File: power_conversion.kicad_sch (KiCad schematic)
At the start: 6 parts, among them U23 AP1117-ADJ

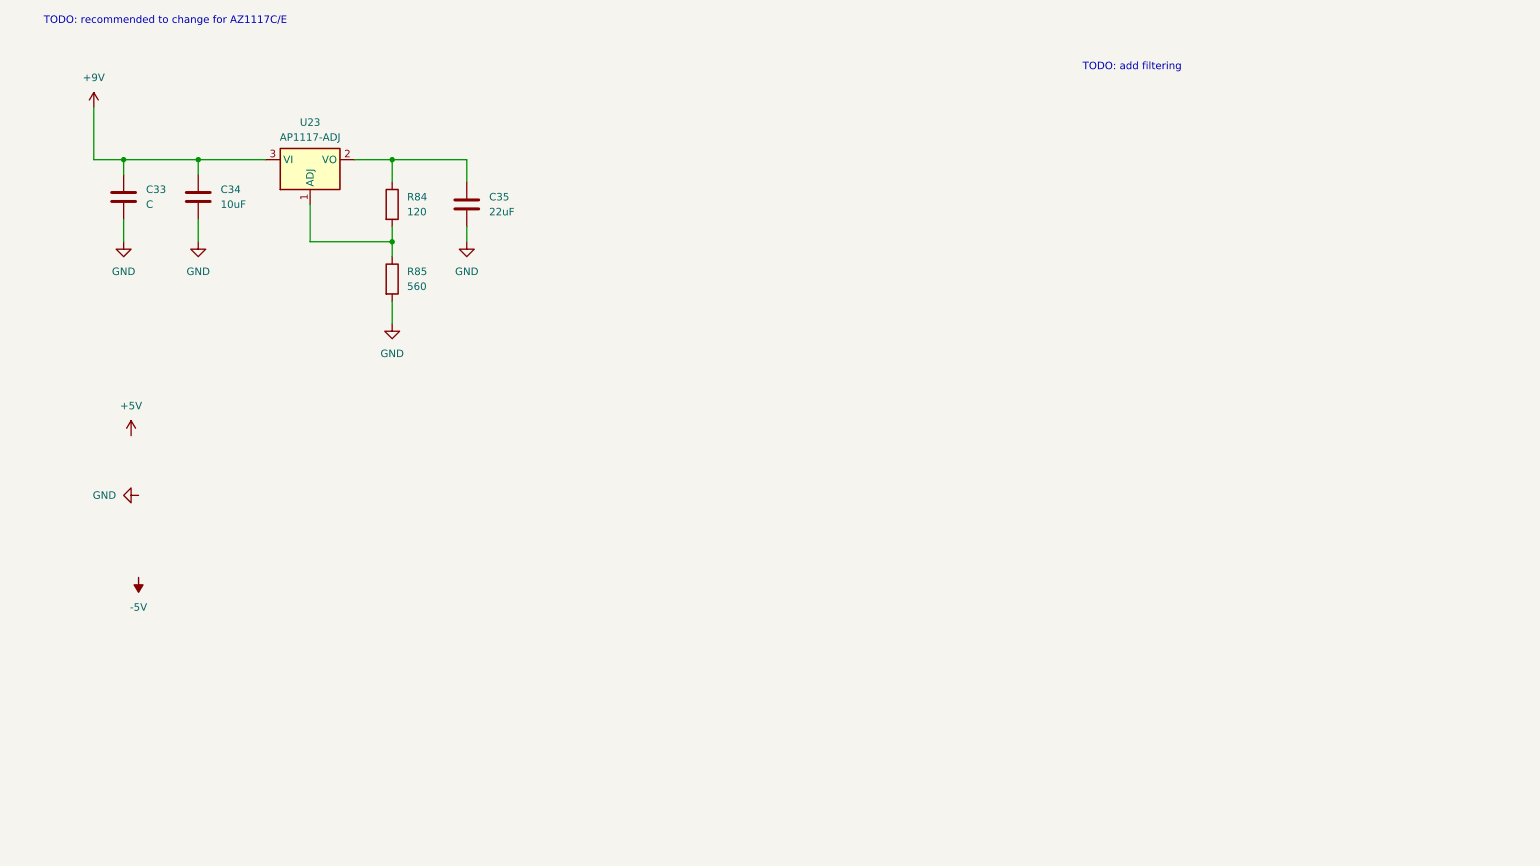
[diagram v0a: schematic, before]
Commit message: PCB edge, initial work on assigning footprints
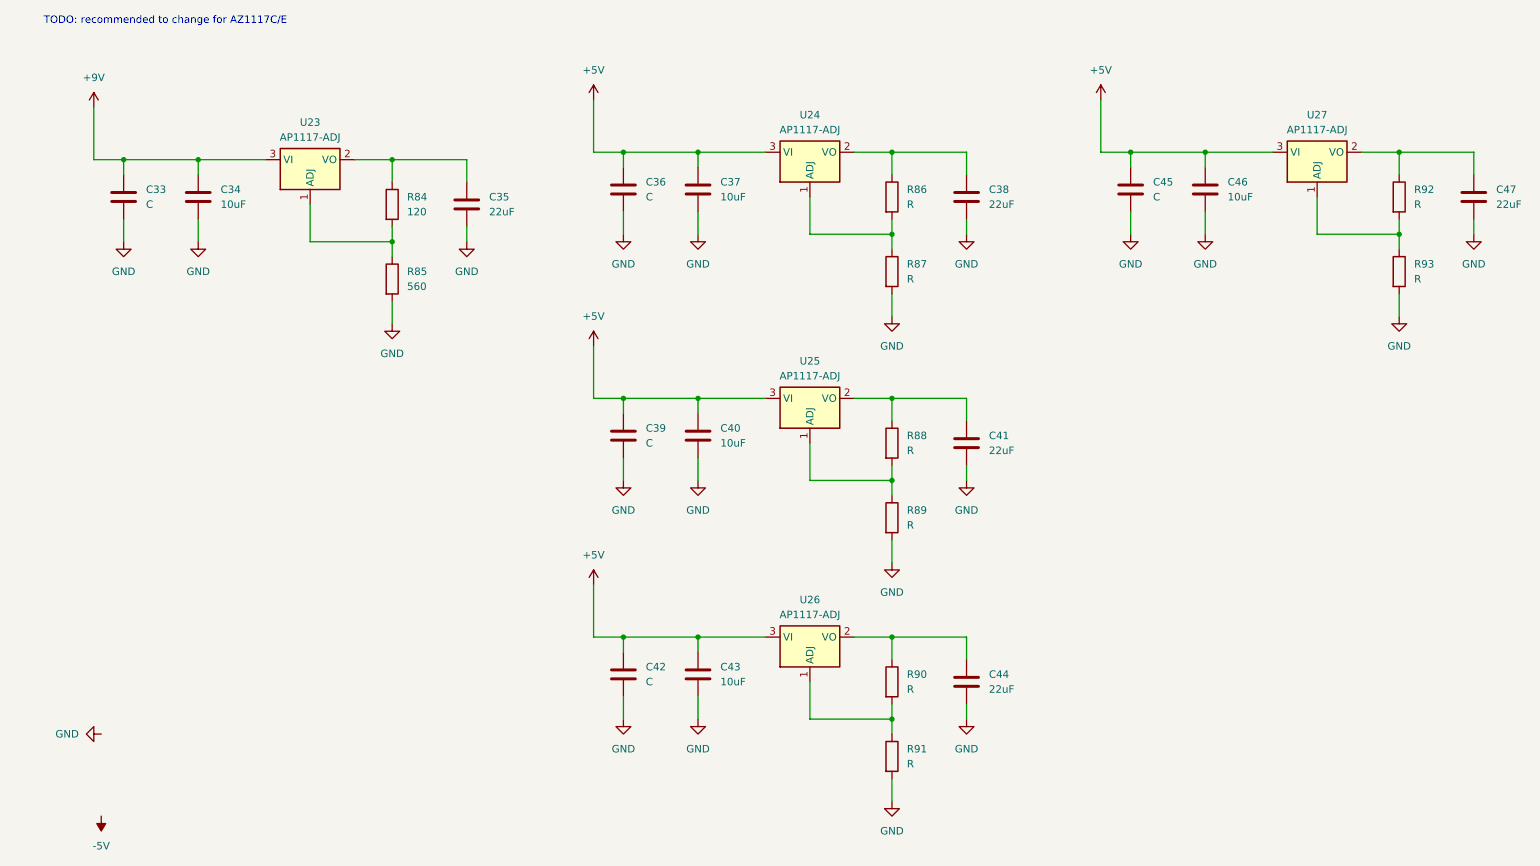
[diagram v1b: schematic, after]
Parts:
- added C36, C39, C42, C45: C, symbol Device:C
- added C37, C40, C43, C46: 10uF, symbol Device:C
- added C38, C41, C44, C47: 22uF, symbol Device:C
- added R86, R87, R88, R89, R90, R91, R92, R93: R, symbol Device:R
- added U24, U25, U26, U27: AP1117-ADJ, Package_TO_SOT_SMD:SOT-223-3_TabPin2, symbol Regulator_Linear:AP1117-ADJ
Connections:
- net +5V: now also C36.1, C37.1, C39.1, C40.1, C42.1, C43.1, C45.1, C46.1, U24.3 (VI), U25.3 (VI), U26.3 (VI), U27.3 (VI)
- net GND: now also C36.2, C37.2, C38.2, C39.2, C40.2, C41.2, C42.2, C43.2, C44.2, C45.2, C46.2, C47.2, R87.2, R89.2, R91.2, R93.2
- new net: R92.2, R93.1, U27.1 (ADJ)
- new net: C47.1, R92.1, U27.2 (VO)
- new net: C44.1, R90.1, U26.2 (VO)
- new net: R90.2, R91.1, U26.1 (ADJ)
- new net: C38.1, R86.1, U24.2 (VO)
- new net: R86.2, R87.1, U24.1 (ADJ)
- new net: R88.2, R89.1, U25.1 (ADJ)
- new net: C41.1, R88.1, U25.2 (VO)
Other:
- note removed: "TODO: add filtering"

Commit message: Add things to MCU on the board
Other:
- note added: "TODO < 0 voltage"
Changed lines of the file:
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@@
 	(generator_version "9.0")
 	(paper "A4")
+	(text "TODO < 0 voltage\n\n"
+		(exclude_from_sim no)
+		(at 34.036 137.16 0)
+		(effects
+			(font
+				(size 1.27 1.27)
+			)
+		)
+	)
 	(text "TODO: recommended to change for AZ1117C/E"
 		(exclude_from_sim no)

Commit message: Mostly finished schematics, without decoupling and power
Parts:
- R84, R85, R86, R87, R88, R89, R90, R91, R92, R93: footprint (none) -> Resistor_SMD:R_1206_3216Metric
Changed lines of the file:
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@@
 			)
 		)
-		(property "Footprint" ""
+		(property "Footprint" "Resistor_SMD:R_1206_3216Metric"
 			(at 165.862 134.62 90)
 			(effects
@@
 			)
 		)
-		(property "Footprint" ""
+		(property "Footprint" "Resistor_SMD:R_1206_3216Metric"
 			(at 252.222 64.77 90)
 			(effects
@@
 			)
 		)
-		(property "Footprint" ""
+		(property "Footprint" "Resistor_SMD:R_1206_3216Metric"
 			(at 165.862 52.07 90)
 			(effects
@@
 			)
 		)
-		(property "Footprint" ""
+		(property "Footprint" "Resistor_SMD:R_1206_3216Metric"
 			(at 165.862 106.68 90)
 			(effects
@@
 			)
 		)
-		(property "Footprint" ""
+		(property "Footprint" "Resistor_SMD:R_1206_3216Metric"
 			(at 80.772 66.04 90)
 			(effects
@@
 			)
 		)
-		(property "Footprint" ""
+		(property "Footprint" "Resistor_SMD:R_1206_3216Metric"
 			(at 165.862 64.77 90)
 			(effects
@@
 			)
 		)
-		(property "Footprint" ""
+		(property "Footprint" "Resistor_SMD:R_1206_3216Metric"
 			(at 252.222 52.07 90)
 			(effects
@@
 			)
 		)
-		(property "Footprint" ""
+		(property "Footprint" "Resistor_SMD:R_1206_3216Metric"
 			(at 80.772 53.34 90)
 			(effects
@@
 			)
 		)
-		(property "Footprint" ""
+		(property "Footprint" "Resistor_SMD:R_1206_3216Metric"
 			(at 165.862 93.98 90)
 			(effects
@@
 			)
 		)
-		(property "Footprint" ""
+		(property "Footprint" "Resistor_SMD:R_1206_3216Metric"
 			(at 165.862 147.32 90)
 			(effects
